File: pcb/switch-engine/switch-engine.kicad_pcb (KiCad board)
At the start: 10 copper layers, 366 parts, among them J1 CONN_PCIE_PWR_8PIN, J10 CORTEX_DEBUG_ETM, J11 SMPM, J12 CONN_01X03, J13 PMOD_HOST, J14 ARF6-08-S-D-A-K-TR, J15 ARF6-08-S-D-A-K-TR, J16 CONN_01X10, J17 ARF6-08-S-D-A-K-TR, J18 ARF6-08-S-D-A-K-TR, J19 CONN_01X10, J2 CONN_IBC_MGMT, J20 0826-1G1T-23-F, J21 ARF6-08-S-D-A-K-TR, J22 ARF6-08-S-D-A-K-TR, J23 CONN_01X10, J24 SMPM, J26 RJ45, J3 CONN_01X03, J4 CORTEX_DEBUG_ETM, J5 FAN_01, J6 FAN_01, J7 JUMPER_0402, J8 XILINX_JTAG, J9 PMOD_HOST, M1 SCREWHOLE, M2 SCREWHOLE, M3 SCREWHOLE, M4 SCREWHOLE, M5 LOGO, M6 LOGO, M7 LOGO, M8 960-27-23-D-AB-0, Q2 SSM6N58NU, SW1 SWITCH, SW2 SWITCH, U1 STM32L431-QFN48, U10 74LVC1T45, U11 74LVC1T45, U12 74LVC1T45, U13 MT25QU256ABA8E12-0AUT, U14 ECS-1612MV-250-CN, U15 SIT9121AI-2BF-XXS156.250000G, U17 AT24MAC402, U18 74LVC1T45, U19 74LVC1T45, U2 MYMGK1R812ERSR, U20 74LVC1T45, U21 74LVC1T45, U22 ECS-1612MV-250-CN, U23 KSZ9031RN, U24 ESD224DQAR, U25 SIT9121AI-2BF-XXS156.250000G, U26 ESD224DQAR, U27 SIT9121AI-2BF-XXS156.250000G, U28 ADP1740ACPZ-2.5-R7, U29 ADM3101E_QFN, U3 MYMGK1R812ERSR, U4 MYMGK00506ERSR, U5 MYMGK00504ERSR, U6 MYMGK00504ERSR, U7 ADP1740ACPZ-1.8-R7, U8 XCKU5P-2FFVB676I, U9 STM32H735-UFBGA176-25

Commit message: Initial rough floorplan
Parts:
- C75, C79: value 2.2 uF -> 4.7 uF; footprint azonenberg_pcb:EIA_0805_CAP_NOSILK -> azonenberg_pcb:EIA_0603_CAP_NOSILK
- moved J26 208.3 mm to (217.7, 6.27), turned to 180 degrees
- moved C37 206.4 mm to (234.2, 67.5)
- moved C148 205.2 mm to (233.0, 78.0)
- moved TP28 204.2 mm to (214.0, 24.0)
- moved C147 191.4 mm to (219.0, 80.5)
- moved C36 191.2 mm to (219.0, 68.5)
- moved C146 188.2 mm to (222.5, 80.5)
- moved C35 188.2 mm to (222.5, 68.5)
- moved TP11 182.6 mm to (239.0, 66.5)
- moved TP24 177.5 mm to (239.5, 77.0)
- moved C150 172.5 mm to (203.0, 21.5)
- moved C151 171.3 mm to (202.5, 24.5)
- moved TP1 171.0 mm to (201.2, 63.8)
- moved C152 170.8 mm to (199.0, 21.5)
- moved C33 169.4 mm to (199.5, 120.0)
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
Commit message: Initial rough FPGA power routing
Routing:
- net /GND: track 0.00 -> 329.2 mm, vias 0 -> 205
- net /1V8: track 0.00 -> 71.0 mm, vias 0 -> 23
- net /FPGA support/VCCINT: track 0.00 -> 53.4 mm, vias 0 -> 40
- net /3V3: track 0.00 -> 30.4 mm, vias 0 -> 6

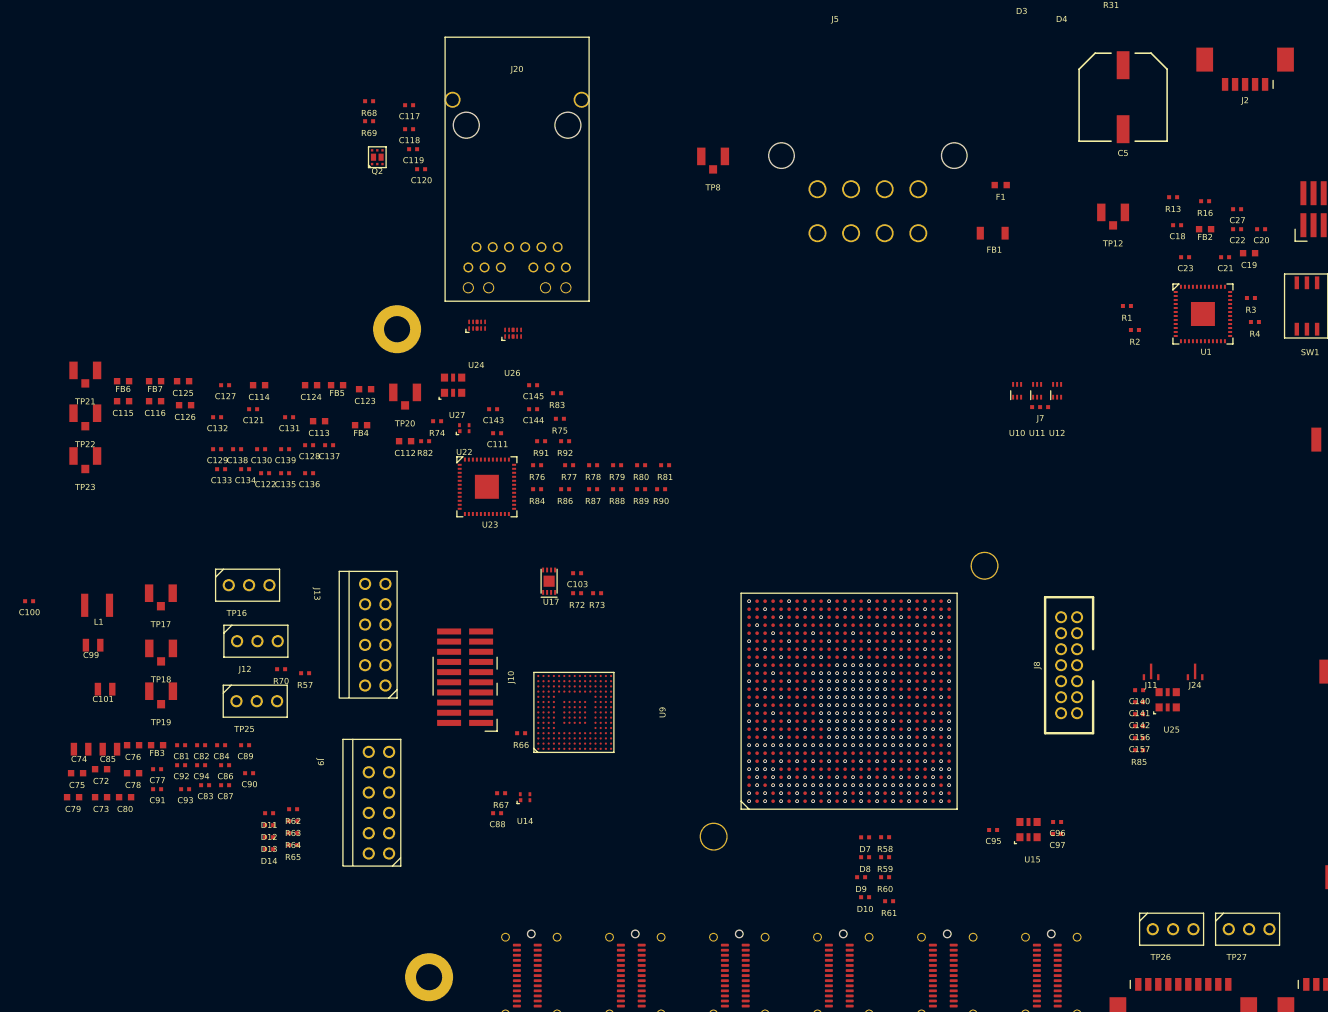
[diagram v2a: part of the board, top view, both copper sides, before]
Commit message: Initial power routing of MCU, breakout for FMC signals on FPGA
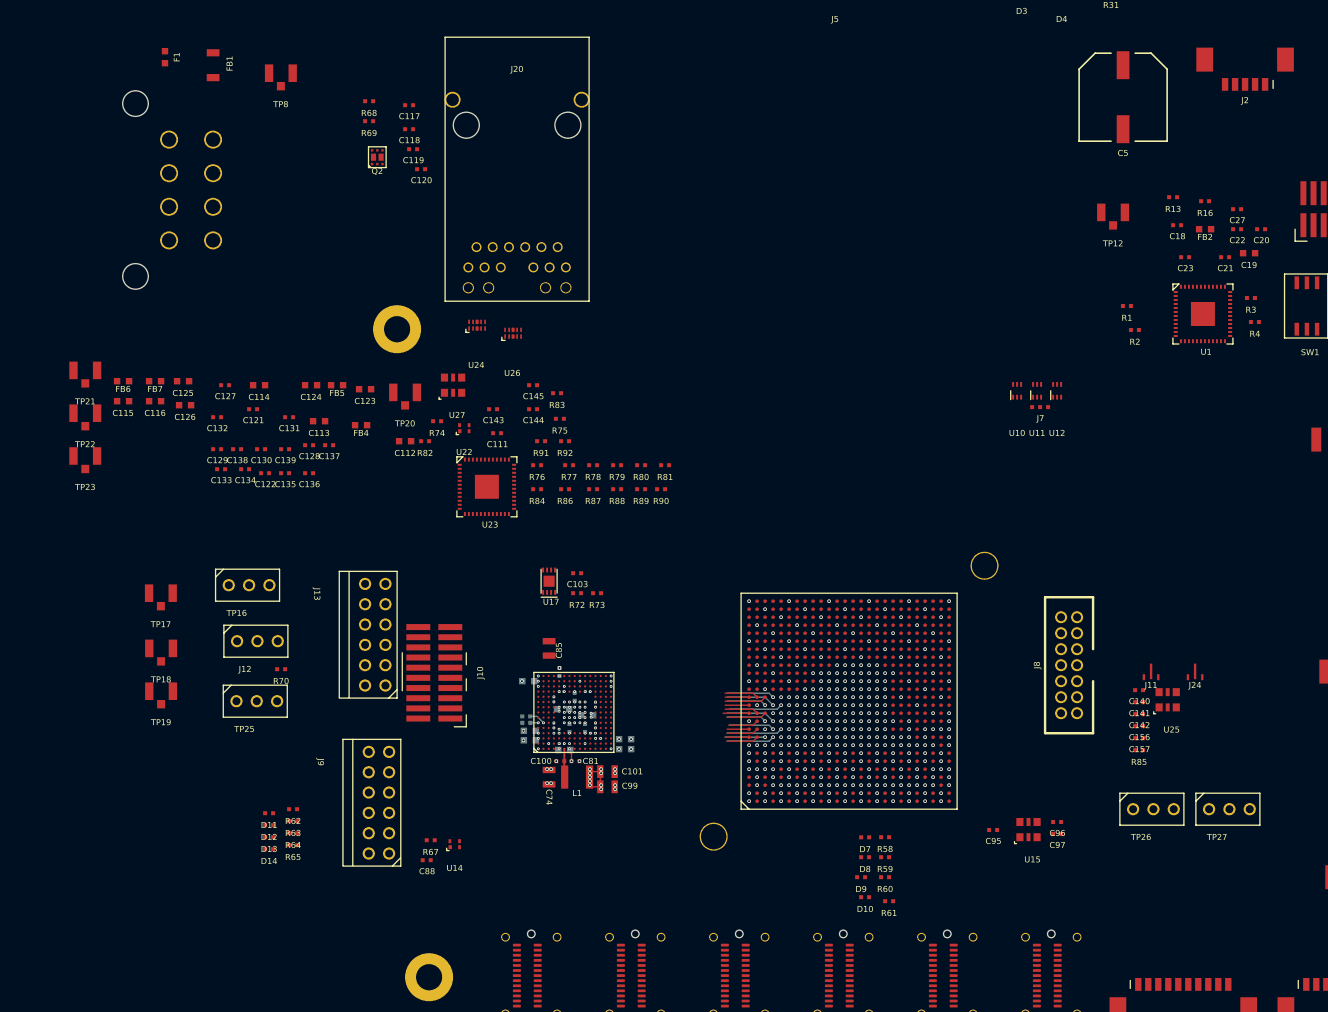
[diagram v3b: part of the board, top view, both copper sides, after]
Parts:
- added C158: 0.47 uF, azonenberg_pcb:EIA_0402_CAP_NOSILK, B.Cu at (62.5, 101.8)
- added C159: 0.47 uF, azonenberg_pcb:EIA_0402_CAP_NOSILK, B.Cu at (59.3, 94.9)
- C72, C73, C75, C76, C78, C79, C80, C87, C91, FB3, R57, R66: moved to B.Cu
- C77, C82, C83, C84, C86, C89, C90, C92, C93, C94: footprint azonenberg_pcb:EIA_0402_CAP_NOSILK -> azonenberg_pcb:EIA_0201_CAP_NOSILK; moved to B.Cu
- moved F1 105.7 mm to (9.99, 18.0), turned to 90 degrees
- moved FB1 99.7 mm to (16.0, 19.0), turned to 90 degrees
- moved J1 87.4 mm to (10.5, 34.6), turned to -90 degrees
- moved C100 69.3 mm to (59.4, 106.0), turned to 180 degrees
- moved C99 66.7 mm to (65.3, 109.2)
- moved L1 63.7 mm to (61.5, 108.0), turned to 180 degrees
- moved C101 63.6 mm to (65.3, 107.3)
- moved C80 62.9 mm to (67.5, 103.2)
- moved C74 58.6 mm to (58.0, 108.0), turned to -90 degrees
- moved FB3 58.5 mm to (67.5, 104.5), turned to 180 degrees
- moved C72 58.2 mm to (59.8, 99.5)
- moved C79 57.7 mm to (55.6, 102.2), turned to 180 degrees
- moved C75 57.6 mm to (55.4, 96.0), turned to 180 degrees
- moved C78 57.2 mm to (62.8, 100.2), turned to 180 degrees
- moved C85 56.3 mm to (58.0, 91.9), turned to 90 degrees
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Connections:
- U8 pad F12: /MCU/FPGA_PMOD_DQ7 -> /MCU/FMC_A19
- U8 pad F13: /MCU/FPGA_PMOD_DQ4 -> /MCU/FMC_AD0
- U8 pad F14: /MCU/FPGA_PMOD_DQ5 -> /MCU/FMC_NE3
- U8 pad G12: /MCU/FPGA_PMOD_DQ1 -> /MCU/FMC_NE1
- U8 pad G14: /MCU/FPGA_PMOD_DQ3 -> /MCU/FMC_AD1
- U8 pad H11: /MCU/FMC_NOE -> /MCU/FPGA_PMOD_DQ2
- U8 pad H14: /MCU/FPGA_PMOD_DQ0 -> /MCU/FMC_NWE
- U8 pad H9: /MCU/FMC_A19 -> /MCU/FPGA_PMOD_DQ7
- U8 pad J10: /MCU/FMC_NE3 -> /MCU/FPGA_PMOD_DQ5
- U8 pad J11: /MCU/FMC_NWE -> /MCU/FPGA_PMOD_DQ0
- U8 pad J14: /MCU/FPGA_PMOD_DQ2 -> /MCU/FPGA_PMOD_DQ6
- U8 pad J15: /MCU/FPGA_PMOD_DQ6 -> /MCU/FMC_NOE
- U8 pad J9: /MCU/FMC_AD0 -> /MCU/FPGA_PMOD_DQ4
- U8 pad K10: /MCU/FMC_AD1 -> /MCU/FPGA_PMOD_DQ3
- U8 pad K9: /MCU/FMC_NE1 -> /MCU/FPGA_PMOD_DQ1
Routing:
- net /GND: track 329.2 -> 563.7 mm, vias 205 -> 261
- net /3V3: track 30.4 -> 81.8 mm, vias 6 -> 29
- net /GTY_VTT: track 0.00 -> 41.5 mm, vias 0 -> 15
- net /MCU/VSMPS: track 0.00 -> 37.7 mm, vias 0 -> 13
- net /FPGA support/GTY_VCC: track 0.00 -> 23.8 mm, vias 0 -> 6
- net /1V8: track 71.0 -> 93.6 mm
- net /FPGA support/GTY_VCCAUX: track 0.00 -> 15.9 mm, vias 0 -> 2
- net /FPGA support/VCCINT: track 53.4 -> 67.6 mm
- net /MCU/FPGA_PMOD_DQ3: track 0.00 -> 11.0 mm, vias 0 -> 1
- net /MCU/FPGA_PMOD_DQ1: track 0.00 -> 10.9 mm, vias 0 -> 1
- net /MCU/FPGA_PMOD_DQ5: track 0.00 -> 10.3 mm, vias 0 -> 1
- net /MCU/FMC_NOE: track 0.00 -> 10.1 mm, vias 0 -> 1
- net /MCU/FPGA_PMOD_DQ4: track 0.00 -> 10.0 mm, vias 0 -> 1
- net /MCU/FPGA_LED_3: track 0.00 -> 9.95 mm, vias 0 -> 1
- net /MCU/FPGA_LED_2: track 0.00 -> 9.85 mm, vias 0 -> 1
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
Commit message: Initial routing progress on RGMII and FMC
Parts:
- C103, C111, C117, C118, C119, C120, C121, C122, C127, C128, C129, C130, C131, C132, C133, C134, C135, C136, C137, C138, C139, C143, C144, C145, Q2, R68, R69, R72, R73, R75, R83, R84, R85, R86, R87, R88, R89, R90, R91, R92: moved to B.Cu
- moved C149 153.6 mm to (41.8, 42.2)
- moved C150 153.6 mm to (50.8, 42.2)
- moved C151 153.6 mm to (50.3, 45.2)
- moved C152 153.6 mm to (46.8, 42.2)
- moved C153 153.6 mm to (46.3, 45.2)
- moved J26 153.6 mm to (65.5, 27.0)
- moved R71 153.6 mm to (37.8, 42.2)
- moved R9 153.6 mm to (41.8, 45.8)
- moved TP28 153.6 mm to (61.8, 44.8)
- moved U29 153.6 mm to (54.8, 43.8)
- moved C127 69.7 mm to (86.2, 70.2)
- moved C132 67.8 mm to (83.8, 71.5), turned to 90 degrees
- moved C133 67.8 mm to (84.8, 70.2), turned to 90 degrees
- moved C129 66.8 mm to (83.2, 66.5), turned to -90 degrees
- moved C134 64.6 mm to (84.5, 66.8), turned to 180 degrees
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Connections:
- U8 pad A10: /MCU/FMC_AD13 -> /MCU/FMC_AD7
- U8 pad A12: /MCU/FMC_AD2 -> /MCU/FMC_AD8
- U8 pad A13: /MCU/FMC_NWAIT -> /MCU/FMC_AD13
- U8 pad A14: /MCU/FMC_A20 -> /MCU/FMC_AD10
- U8 pad A18: /RGMII PHY/RGMII_TXD3 -> unconnected-(U8D-IO_L16N_T2U_N7_QBC_AD3N_67-PadA18)
- U8 pad A19: /RGMII PHY/RGMII_TX_CLK -> /RGMII PHY/RGMII_TXD1
- U8 pad A20: /RGMII PHY/ETH_LED1_N_1V8 -> /RGMII PHY/RGMII_TXD2
- U8 pad A22: unconnected-(U8D-IO_L19P_T3L_N0_DBC_AD9P_67-PadA22) -> /RGMII PHY/RGMII_TX_EN
- U8 pad A24: unconnected-(U8D-IO_L23P_T3U_N8_67-PadA24) -> /RGMII PHY/ETH_RXD1
- U8 pad A25: unconnected-(U8D-IO_L23N_T3U_N9_67-PadA25) -> /RGMII PHY/ETH_RXD0
- U8 pad A9: /MCU/FMC_AD10 -> /MCU/FMC_AD5
- U8 pad B10: /MCU/FMC_AD12 -> /MCU/FMC_AD4
- U8 pad B11: /MCU/FMC_A18 -> /MCU/FMC_AD6
- U8 pad B12: /MCU/FMC_NE2 -> /MCU/FMC_AD12
- U8 pad B14: /MCU/FMC_A21 -> /MCU/FMC_AD14
- U8 pad B15: /RGMII PHY/RGMII_TXD1 -> unconnected-(U8D-IO_L17P_T2U_N8_AD10P_67-PadB15)
- U8 pad B16: /RGMII PHY/RGMII_TXD0 -> unconnected-(U8D-IO_T2U_N12_67-PadB16)
- U8 pad B20: /RGMII PHY/RGMII_TXD2 -> /RGMII PHY/RGMII_TXD3
- U8 pad B21: unconnected-(U8D-IO_L22N_T3U_N7_DBC_AD0N_67-PadB21) -> /RGMII PHY/RGMII_TX_CLK
- U8 pad B22: unconnected-(U8D-IO_L24N_T3U_N11_67-PadB22) -> /RGMII PHY/ETH_RXD3
- U8 pad B24: /RGMII PHY/RGMII_TX_EN -> /RGMII PHY/ETH_RX_DV
- U8 pad C11: /MCU/FMC_AD11 -> /MCU/FMC_AD1
- U8 pad C12: /MCU/FMC_AD3 -> /MCU/FMC_AD11
- U8 pad C13: /MCU/FMC_A24 -> /MCU/FMC_NE1
- U8 pad C14: /MCU/FMC_NL_NADV -> /MCU/FMC_AD15
- U8 pad C17: /RGMII PHY/ETH_RST_N -> unconnected-(U8D-IO_L15P_T2L_N4_AD11P_67-PadC17)
- U8 pad C19: /RGMII PHY/ETH_MDIO -> unconnected-(U8D-IO_L13N_T2L_N1_GC_QBC_67-PadC19)
- U8 pad C21: unconnected-(U8D-IO_L22P_T3U_N6_DBC_AD0P_67-PadC21) -> /RGMII PHY/ETH_LED2_N_1V8_INV
- U8 pad C22: unconnected-(U8D-IO_L24P_T3U_N10_67-PadC22) -> /RGMII PHY/ETH_MDC
- U8 pad C23: /RGMII PHY/ETH_LED1_N_1V8_INV -> /RGMII PHY/RGMII_TXD0
- U8 pad C9: /MCU/FMC_AD5 -> /MCU/FMC_A16
- U8 pad D10: /MCU/FMC_AD8 -> /MCU/FMC_AD0
- U8 pad D11: /MCU/FMC_A25 -> /MCU/FMC_NE3
- U8 pad D13: /MCU/FMC_AD15 -> /MCU/FMC_NL_NADV
- U8 pad D18: /RGMII PHY/ETH_RXD1 -> unconnected-(U8D-IO_L11N_T1U_N9_GC_67-PadD18)
- U8 pad D21: /RGMII PHY/ETH_LED2_N_1V8_INV -> /RGMII PHY/ETH_MDIO
- U8 pad D9: /MCU/FMC_AD6 -> /MCU/FMC_A17
- U8 pad E10: /MCU/FMC_A22 -> /MCU/FMC_A18
- U8 pad E12: /MCU/FMC_AD7 -> /MCU/FMC_NE2
- U8 pad E13: /MCU/FMC_AD4 -> /MCU/FMC_NWAIT
- U8 pad E20: unconnected-(U8D-IO_L10N_T1U_N7_QBC_AD4N_67-PadE20) -> /RGMII PHY/ETH_LED2_N_1V8
- U8 pad E21: /RGMII PHY/ETH_RXD3 -> /RGMII PHY/ETH_LED1_N_1V8_INV
- U8 pad E22: unconnected-(U8D-IO_T3U_N12_67-PadE22) -> /RGMII PHY/ETH_RST_N
- U8 pad F10: /MCU/FMC_A17 -> /MCU/FMC_A22
- U8 pad F13: /MCU/FMC_AD0 -> /MCU/FMC_AD2
- U8 pad F14: /MCU/FMC_NE3 -> /MCU/FMC_A25
- U8 pad F18: /RGMII PHY/ETH_RXD0 -> unconnected-(U8D-IO_L8P_T1L_N2_AD5P_67-PadF18)
- U8 pad F19: /RGMII PHY/ETH_LED2_N_1V8 -> unconnected-(U8D-IO_L8N_T1L_N3_AD5N_67-PadF19)
- U8 pad F9: /MCU/FMC_A16 -> /MCU/FMC_A20
- U8 pad G12: /MCU/FMC_NE1 -> /MCU/FMC_A24
- U8 pad G14: /MCU/FMC_AD1 -> /MCU/FMC_AD3
- U8 pad G20: /RGMII PHY/ETH_RX_DV -> unconnected-(U8D-IO_L9P_T1L_N4_AD12P_67-PadG20)
- U8 pad G21: unconnected-(U8D-IO_L9N_T1L_N5_AD12N_67-PadG21) -> /RGMII PHY/ETH_LED1_N_1V8
- U8 pad G9: /MCU/FMC_AD14 -> /MCU/FMC_A21
- U8 pad H19: /RGMII PHY/ETH_MDC -> unconnected-(U8D-IO_L7N_T1L_N1_QBC_AD13N_67-PadH19)
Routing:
- net /GND: track 563.7 -> 867.7 mm, vias 261 -> 375
- net /3V3: track 81.8 -> 180.2 mm, vias 29 -> 37
- net /MCU/FMC_NWAIT: track 3.00 -> 38.7 mm, vias 0 -> 2
- net /MCU/FMC_A18: track 3.71 -> 36.5 mm, vias 0 -> 2
- net /1V8: track 93.6 -> 124.8 mm, vias 23 -> 29
- net /MCU/FMC_NE3: track 6.87 -> 37.2 mm, vias 1 -> 2
- net /MCU/FMC_AD1: track 8.05 -> 38.1 mm, vias 1 -> 2
- net /MCU/FMC_AD0: track 6.87 -> 36.5 mm, vias 1 -> 2
- net /MCU/FMC_A16: track 6.57 -> 35.4 mm, vias 1 -> 2
- net /MCU/FMC_NE1: track 7.87 -> 36.0 mm, vias 1 -> 2
- net /RGMII PHY/RGMII_TXD1: track 0.00 -> 27.7 mm
- net /MCU/FMC_A17: track 7.03 -> 34.4 mm, vias 1 -> 2
- net /RGMII PHY/RGMII_TXD0: track 0.00 -> 26.5 mm, vias 0 -> 2
- net /RGMII PHY/RGMII_TXD2: track 0.00 -> 25.7 mm
- net /RGMII PHY/RGMII_TXD3: track 0.00 -> 25.2 mm
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
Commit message: Lots of progress routing ARC6s
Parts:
- C104, C105, C106, C107, C108, C109, C110, C58, C59, C60, C61, C62, C63, C95, C96, C97, C98, D3, D4, D5, D6, R31, R38, R39, R40, R41, R43, U15, U18, U19, U20, U21: moved to B.Cu
- moved C64 103.3 mm to (113.0, 55.8)
- moved C65 102.7 mm to (112.5, 57.8)
- moved C66 102.7 mm to (112.5, 59.2)
- moved C67 102.7 mm to (112.5, 60.8)
- moved C68 102.7 mm to (112.5, 62.2)
- moved C69 102.7 mm to (112.5, 63.8)
- moved R43 60.8 mm to (103.0, 102.5), turned to 180 degrees
- moved R41 59.5 mm to (109.3, 102.5)
- moved R40 58.0 mm to (103.5, 101.0), turned to 180 degrees
- moved R39 54.6 mm to (101.0, 102.5), turned to -90 degrees
- moved C39 50.6 mm to (116.8, 46.0)
- moved C96 50.3 mm to (71.8, 106.5), turned to 180 degrees
- moved C97 50.3 mm to (71.8, 108.0), turned to 180 degrees
- moved J6 48.4 mm to (114.0, 39.0)
- moved C63 46.9 mm to (99.0, 105.5), turned to -90 degrees
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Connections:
- U8 pad AA4: /Line card interfaces/LC0_PHY0_LANE0_TX_N -> /Line card interfaces/LC0_PHY0_LANE0_TX_P
- U8 pad AA5: /Line card interfaces/LC0_PHY0_LANE0_TX_P -> /Line card interfaces/LC0_PHY0_LANE0_TX_N
- U8 pad AB1: /SFP28 interfaces/GTY3_RX_N -> /SFP28 interfaces/GTY2_RX_P
- U8 pad AB2: /SFP28 interfaces/GTY3_RX_P -> /SFP28 interfaces/GTY2_RX_N
- U8 pad AC4: /SFP28 interfaces/GTY3_TX_N -> /SFP28 interfaces/GTY2_TX_N
- U8 pad AC5: /SFP28 interfaces/GTY3_TX_P -> /SFP28 interfaces/GTY2_TX_P
- U8 pad AD1: /SFP28 interfaces/GTY2_RX_N -> /SFP28 interfaces/GTY3_RX_P
- U8 pad AD2: /SFP28 interfaces/GTY2_RX_P -> /SFP28 interfaces/GTY3_RX_N
- U8 pad AD6: /SFP28 interfaces/GTY2_TX_N -> /SFP28 interfaces/GTY3_TX_N
- U8 pad AD7: /SFP28 interfaces/GTY2_TX_P -> /SFP28 interfaces/GTY3_TX_P
- U8 pad AE3: /SFP28 interfaces/SFP28_1_RX_N -> /SFP28 interfaces/SFP28_0_RX_N
- U8 pad AE4: /SFP28 interfaces/SFP28_1_RX_P -> /SFP28 interfaces/SFP28_0_RX_P
- U8 pad AE8: /SFP28 interfaces/SFP28_1_TX_N -> /SFP28 interfaces/SFP28_0_TX_N
- U8 pad AE9: /SFP28 interfaces/SFP28_1_TX_P -> /SFP28 interfaces/SFP28_0_TX_P
- U8 pad AF1: /SFP28 interfaces/SFP28_0_RX_N -> /SFP28 interfaces/SFP28_1_RX_N
- U8 pad AF2: /SFP28 interfaces/SFP28_0_RX_P -> /SFP28 interfaces/SFP28_1_RX_P
- U8 pad AF6: /SFP28 interfaces/SFP28_0_TX_N -> /SFP28 interfaces/SFP28_1_TX_N
- U8 pad AF7: /SFP28 interfaces/SFP28_0_TX_P -> /SFP28 interfaces/SFP28_1_TX_P
- U8 pad R4: /Line card interfaces/LC0_PHY1_LANE0_TX_N -> /Line card interfaces/LC0_PHY1_LANE0_TX_P
- U8 pad R5: /Line card interfaces/LC0_PHY1_LANE0_TX_P -> /Line card interfaces/LC0_PHY1_LANE0_TX_N
- U8 pad T1: /Line card interfaces/LC0_PHY0_LANE2_RX_N -> /Line card interfaces/LC0_PHY0_LANE2_RX_P
- U8 pad T2: /Line card interfaces/LC0_PHY0_LANE2_RX_P -> /Line card interfaces/LC0_PHY0_LANE2_RX_N
- U8 pad U4: /Line card interfaces/LC0_PHY0_LANE2_TX_N -> /Line card interfaces/LC0_PHY0_LANE2_TX_P
- U8 pad U5: /Line card interfaces/LC0_PHY0_LANE2_TX_P -> /Line card interfaces/LC0_PHY0_LANE2_TX_N
- U8 pad W4: /Line card interfaces/LC0_PHY0_LANE1_TX_N -> /Line card interfaces/LC0_PHY0_LANE1_TX_P
- U8 pad W5: /Line card interfaces/LC0_PHY0_LANE1_TX_P -> /Line card interfaces/LC0_PHY0_LANE1_TX_N
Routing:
- net /GND: track 867.7 -> 1061.4 mm, vias 375 -> 396
- net /3V3: track 180.2 -> 312.3 mm, vias 37 -> 42
- net /SFP28 interfaces/SFP28_0_TX_P: track 3.37 -> 54.5 mm
- net /SFP28 interfaces/SFP28_0_TX_N: track 3.37 -> 54.5 mm
- net /SFP28 interfaces/SFP28_0_RX_P: track 2.57 -> 53.4 mm, vias 0 -> 2
- net /SFP28 interfaces/SFP28_0_RX_N: track 2.57 -> 53.4 mm, vias 0 -> 2
- net /SFP28 interfaces/SFP28_1_RX_P: track 2.92 -> 46.1 mm, vias 0 -> 2
- net /SFP28 interfaces/SFP28_1_RX_N: track 2.92 -> 46.0 mm, vias 0 -> 2
- net /SFP28 interfaces/SFP28_1_TX_P: track 4.97 -> 47.5 mm
- net /SFP28 interfaces/SFP28_1_TX_N: track 4.97 -> 47.5 mm
- net /Line card interfaces/LC0_PHY1_LANE0_RX_N: track 3.38 -> 39.1 mm, vias 0 -> 2
- net /Line card interfaces/LC0_PHY1_LANE0_RX_P: track 4.51 -> 39.4 mm, vias 0 -> 2
- net /Line card interfaces/LC0_PHY1_LANE0_TX_N: track 4.92 -> 39.5 mm, vias 1 -> 0
- net /Line card interfaces/LC0_PHY1_LANE0_TX_P: track 5.99 -> 39.4 mm, vias 1 -> 0
- net /SFP28 interfaces/GTY3_TX_P: track 5.17 -> 37.6 mm, vias 0 -> 2
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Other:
- board outline added: 124 x 112 mm
- board text added: "FAN1"
- board text added: "FAN2"
- board text added: "GND"
- board text added: "LINE CARD 0 MGMT"
- board text added: "LINE CARD 1 MGMT"
- board text added: "SFP0_SCL"
- board text added: "SFP0_SDA"
- board text added: "SFP1_SCL"
- board text added: "SFP1_SDA"
- board text added: "SFP28 I2C"

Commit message: Progress on GTY routing
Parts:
- C102, C154, C155, C45, C48, C50, C51, C57: moved to B.Cu
- moved C155 61.5 mm to (115.0, 96.8), turned to 90 degrees
- moved C48 59.6 mm to (112.8, 96.8), turned to 90 degrees
- moved C50 57.4 mm to (112.8, 101.8), turned to -90 degrees
- moved C57 56.5 mm to (112.8, 93.5), turned to 90 degrees
- moved C154 55.5 mm to (117.2, 101.8), turned to -90 degrees
- moved C45 54.6 mm to (110.5, 93.5), turned to 90 degrees
- moved C102 52.2 mm to (115.0, 101.8), turned to -90 degrees
- moved C51 50.2 mm to (110.5, 96.8), turned to 90 degrees
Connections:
- U8 pad C3: /Line card interfaces/LC1_PHY1_LANE0_RX_N -> /Line card interfaces/LC1_PHY0_LANE2_RX_N
- U8 pad C4: /Line card interfaces/LC1_PHY1_LANE0_RX_P -> /Line card interfaces/LC1_PHY0_LANE2_RX_P
- U8 pad D1: /Line card interfaces/LC1_PHY0_LANE2_RX_N -> /Line card interfaces/LC1_PHY1_LANE0_RX_N
- U8 pad D2: /Line card interfaces/LC1_PHY0_LANE2_RX_P -> /Line card interfaces/LC1_PHY1_LANE0_RX_P
- U8 pad E4: /Line card interfaces/LC1_PHY1_LANE0_TX_N -> /Line card interfaces/LC1_PHY0_LANE2_TX_P
- U8 pad E5: /Line card interfaces/LC1_PHY1_LANE0_TX_P -> /Line card interfaces/LC1_PHY0_LANE2_TX_N
- U8 pad F6: /Line card interfaces/LC1_PHY0_LANE2_TX_N -> /Line card interfaces/LC1_PHY1_LANE0_TX_N
- U8 pad F7: /Line card interfaces/LC1_PHY0_LANE2_TX_P -> /Line card interfaces/LC1_PHY1_LANE0_TX_P
- U8 pad G4: /Line card interfaces/LC1_PHY0_LANE1_TX_N -> /Line card interfaces/LC1_PHY0_LANE1_TX_P
- U8 pad G5: /Line card interfaces/LC1_PHY0_LANE1_TX_P -> /Line card interfaces/LC1_PHY0_LANE1_TX_N
- U8 pad J4: /Line card interfaces/LC1_PHY0_LANE0_TX_N -> /Line card interfaces/LC1_PHY0_LANE0_TX_P
- U8 pad J5: /Line card interfaces/LC1_PHY0_LANE0_TX_P -> /Line card interfaces/LC1_PHY0_LANE0_TX_N
- U8 pad L4: /Line card interfaces/LC0_PHY1_LANE2_TX_N -> /Line card interfaces/LC0_PHY1_LANE2_TX_P
- U8 pad L5: /Line card interfaces/LC0_PHY1_LANE2_TX_P -> /Line card interfaces/LC0_PHY1_LANE2_TX_N
- U8 pad N4: /Line card interfaces/LC0_PHY1_LANE1_TX_N -> /Line card interfaces/LC0_PHY1_LANE1_TX_P
- U8 pad N5: /Line card interfaces/LC0_PHY1_LANE1_TX_P -> /Line card interfaces/LC0_PHY1_LANE1_TX_N
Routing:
- net /Line card interfaces/LC1_PHY0_LANE0_TX_N: track 4.17 -> 44.9 mm, vias 1 -> 0
- net /Line card interfaces/LC1_PHY0_LANE0_TX_P: track 5.24 -> 44.9 mm, vias 1 -> 0
- net /Line card interfaces/LC1_PHY0_LANE1_TX_N: track 7.67 -> 41.3 mm, vias 1 -> 0
- net /Line card interfaces/LC1_PHY0_LANE1_TX_P: track 7.67 -> 41.2 mm, vias 1 -> 0
- net /Line card interfaces/LC0_PHY1_LANE1_RX_N: track 2.87 -> 34.9 mm, vias 0 -> 2
- net /Line card interfaces/LC0_PHY1_LANE1_RX_P: track 4.15 -> 35.0 mm, vias 0 -> 2
- net /Line card interfaces/LC0_PHY1_LANE1_TX_N: track 4.17 -> 34.8 mm, vias 1 -> 0
- net /Line card interfaces/LC1_PHY0_LANE2_TX_N: track 6.96 -> 37.4 mm, vias 1 -> 0
- net /Line card interfaces/LC1_PHY0_LANE2_TX_P: track 7.62 -> 37.3 mm, vias 1 -> 0
- net /Line card interfaces/LC0_PHY1_LANE1_TX_P: track 5.24 -> 34.7 mm, vias 1 -> 0
- net /Line card interfaces/LC0_PHY1_LANE2_RX_N: track 3.53 -> 31.2 mm, vias 0 -> 2
- net /Line card interfaces/LC0_PHY1_LANE2_TX_N: track 3.92 -> 31.2 mm, vias 1 -> 0
- net /Line card interfaces/LC0_PHY1_LANE2_RX_P: track 4.66 -> 31.3 mm, vias 0 -> 2
- net /Line card interfaces/LC0_PHY1_LANE2_TX_P: track 4.99 -> 31.2 mm, vias 1 -> 0
- net /FPGA support/FPGA_RESET_N: track 4.96 -> 16.3 mm
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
